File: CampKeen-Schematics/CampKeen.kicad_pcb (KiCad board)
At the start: 4 copper layers, 193.7 x 142.2 mm, 326 parts, among them IC1 CD74HC4050ME4, IC10 SN7404DR, IC11 LTV-814, IC12 LTV-814, IC2 LM2597MX-ADJ_NOPB, IC3 LM2670SX-5.0_NOPB, IC4 DS3231SN#, IC5 OPA2340PA, IC6 OPA2340PA, IC7 SN7404DR, IC8 SN7404DR, IC9 SN7404DR, J1 Vin, J2 Conn_01x02, J3 CircuitSetupsSplitPhase, J4 Conn_01x02, J5 Conn_01x02, J6 Conn_01x02, J7 GenEnclosure, J8 GenHeadL, J9 GenHeadR, P1 Power, P10 CONN_01X01, P11 CONN_01X01, P12 CONN_01X01, P13 CONN_01X01, P2 Analog, P3 Analog, P4 Digital, P5 PWM, P6 PWM, P7 Communication, P8 CONN_01X01, P9 CONN_01X01, Q1 IRF9Z34NPBF, Q10 2N7000, Q11 IRF9Z34NPBF, Q12 2N7000, Q13 2N7000, Q14 2N7000, Q15 2N7000, Q16 2N7000, Q17 2N7000, Q18 2N7000, Q19 2N7000, Q2 2N7000, Q20 2N7000, Q21 2N7000, Q22 2N7000, Q23 2N7000, Q24 2N7000, Q25 2N7000, Q26 2N7000, Q27 2N7000, Q28 2N7000, Q29 2N7000, Q3 IRF9Z34NPBF, Q30 2N7000, Q31 2N7000, Q32 IRF9Z34NPBF, Q33 IRF9Z34NPBF, Q34 2N7000, Q35 IRF9Z34NPBF, Q36 2N7000, Q37 IRF9Z34NPBF, Q38 2N7000, Q39 IRF9Z34NPBF, Q4 2N7000, Q40 2N7000, Q41 IRF9Z34NPBF, Q42 2N7000, Q43 2N7000, Q44 IRF9Z34NPBF, Q45 IRF9Z34NPBF, Q46 2N7000, Q47 IRF9Z34NPBF, Q48 2N7000, Q49 IRF9Z34NPBF, Q5 2N7000, Q50 2N7000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

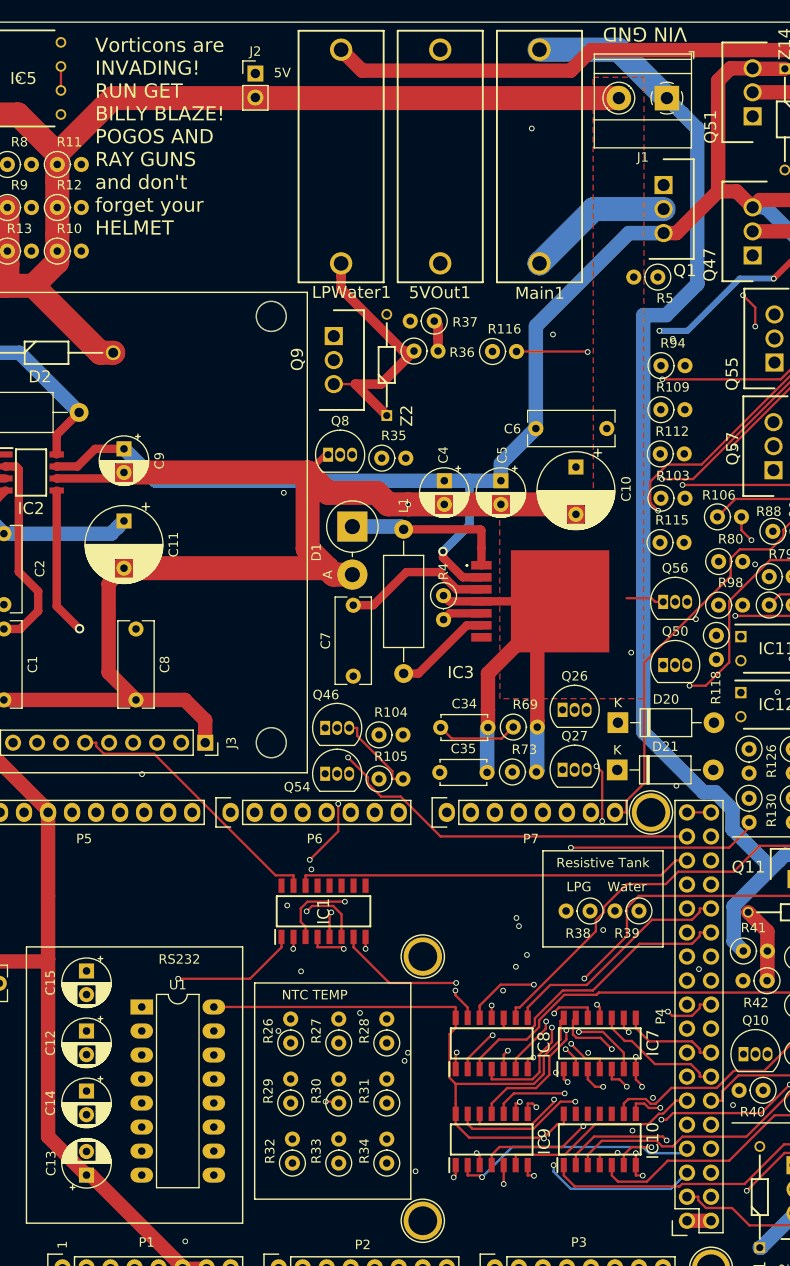
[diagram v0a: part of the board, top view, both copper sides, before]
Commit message: working on fixing some traces for the next HW build.
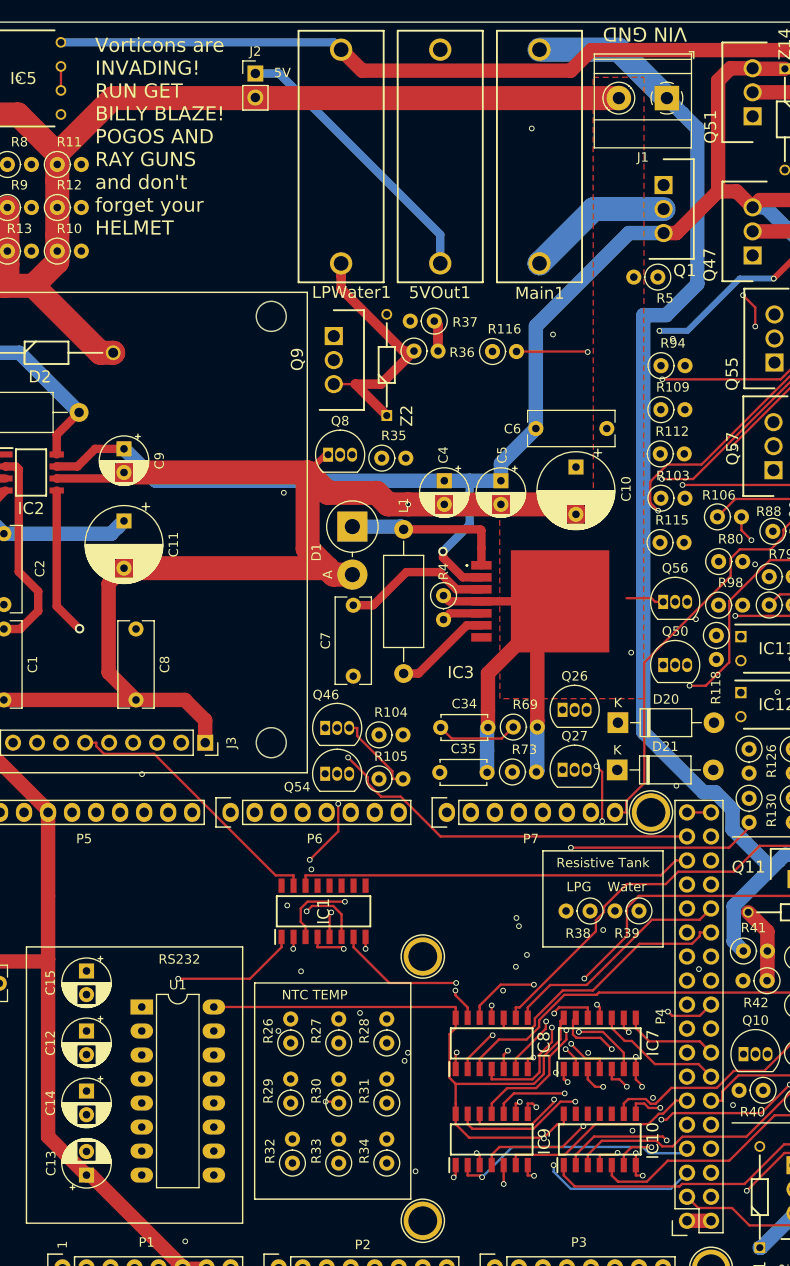
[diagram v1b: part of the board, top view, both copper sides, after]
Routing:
- net +5V: track 844.5 -> 870.3 mm

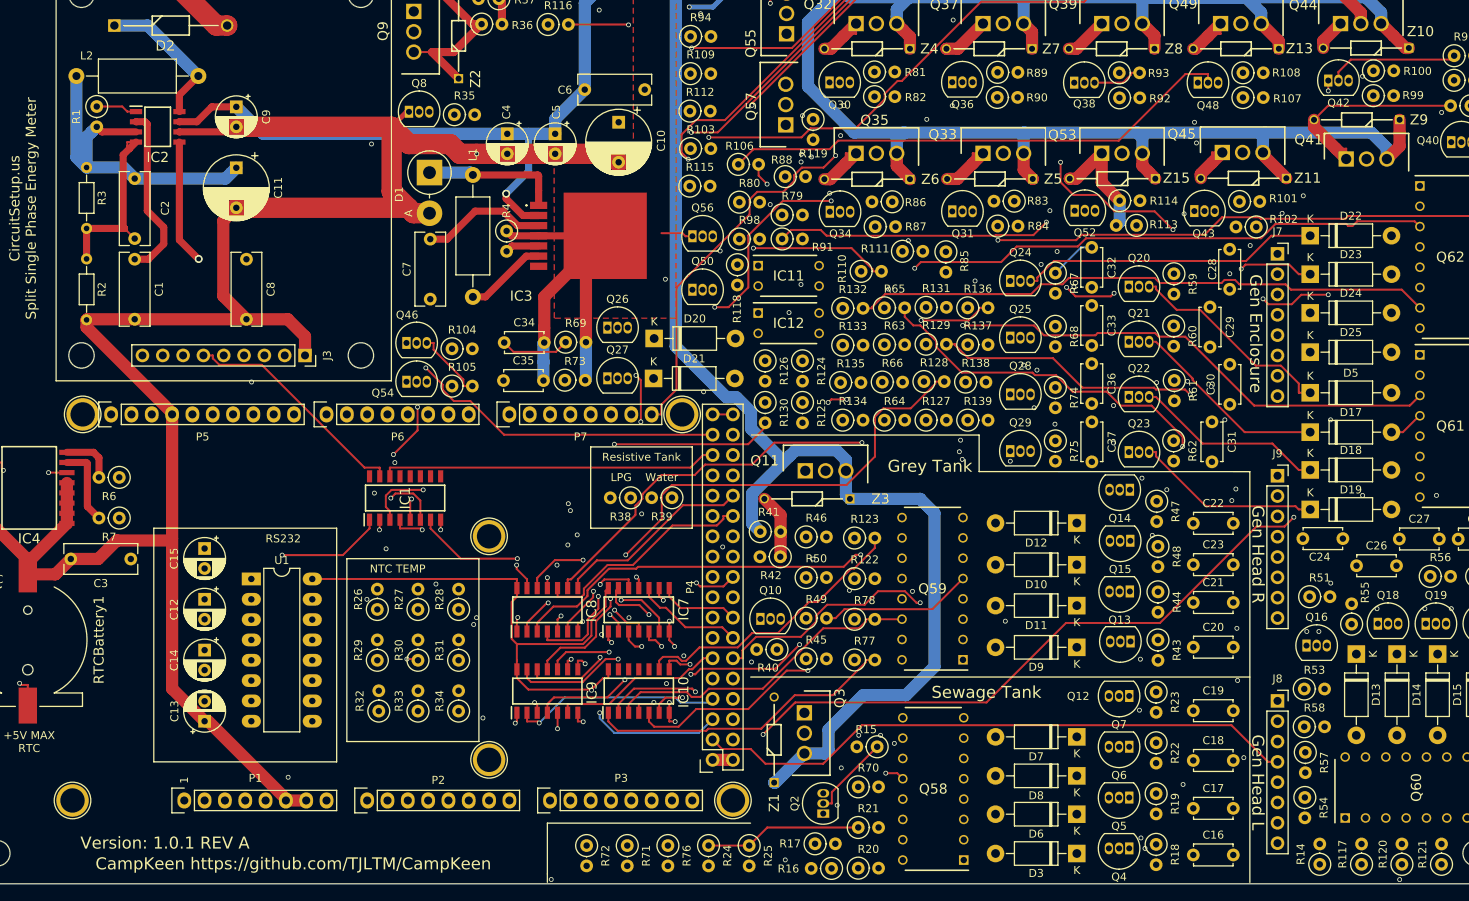
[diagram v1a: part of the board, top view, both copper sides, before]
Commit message: removing the old fab file zips, updated PCB to 1.0.1 Rev B and adding the new fab files.
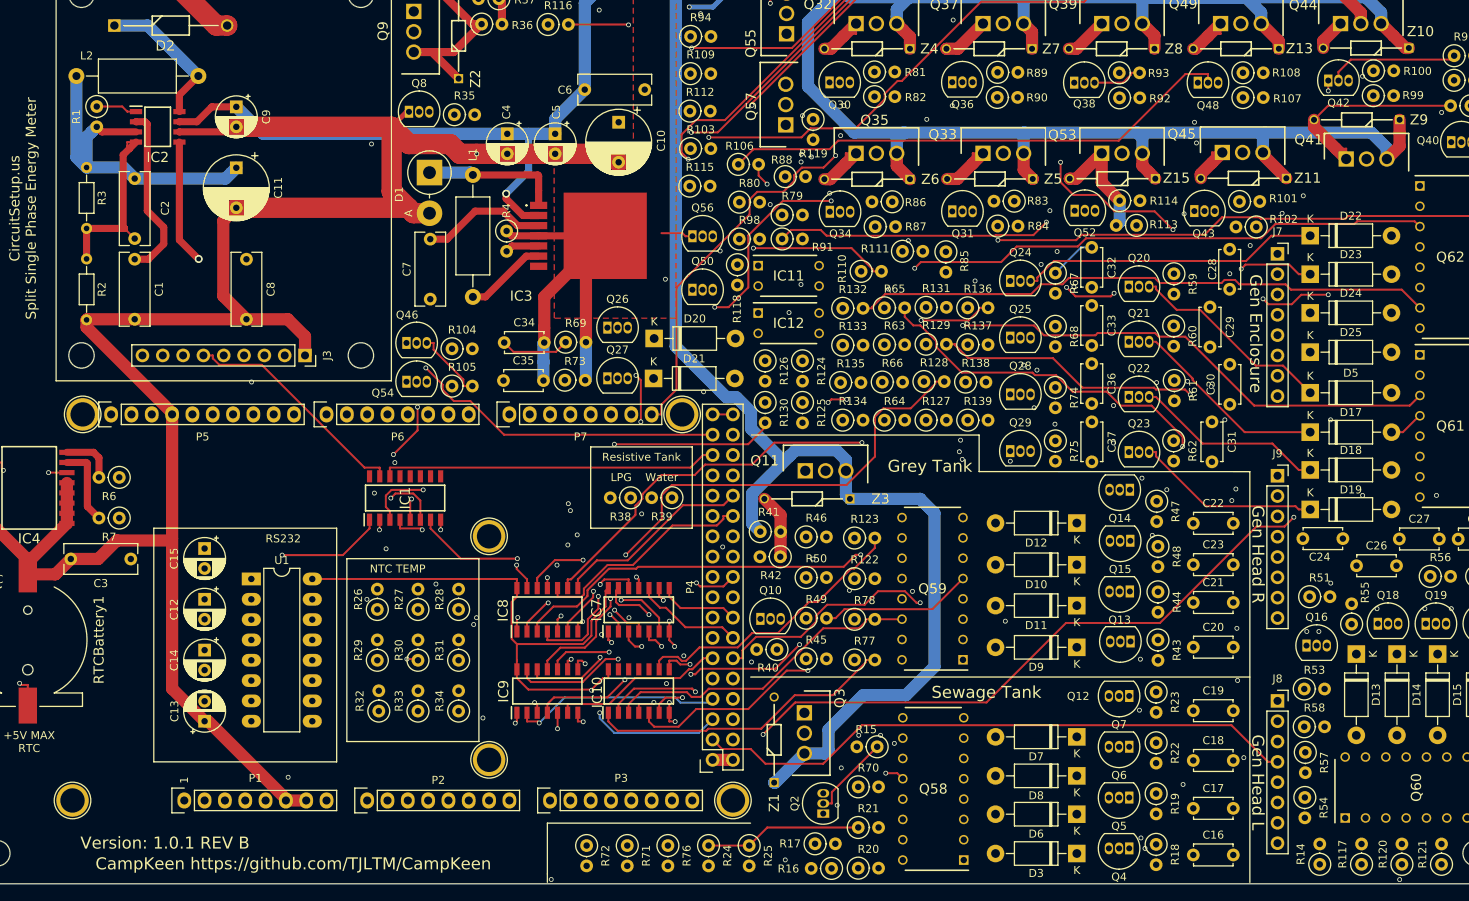
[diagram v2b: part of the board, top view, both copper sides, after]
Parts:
- IC10, IC7, IC8, IC9: footprint Samac_Sys:SOIC127P600X175-14N -> SamacSys_Parts:SOIC127P600X175-14N
- IC11, IC12: footprint Samac_Sys:DIP762W60P254L460H450Q4N -> SamacSys_Parts:DIP762W60P254L460H450Q4N
- Q58, Q59, Q60, Q61, Q62: footprint Samac_Sys:DIP762W60P254L1984H450Q16N -> SamacSys_Parts:DIP762W60P254L1984H450Q16N
- R6, R7: value 47k -> 10k
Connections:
- net AUXVoltage renamed GenFuelPressure
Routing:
- net Net-(D5-Pad1): track 26.5 -> 25.8 mm
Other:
- board text added: "Version: 1.0.1 REV B"
- board text removed: "Version: 1.0.1 REV A"

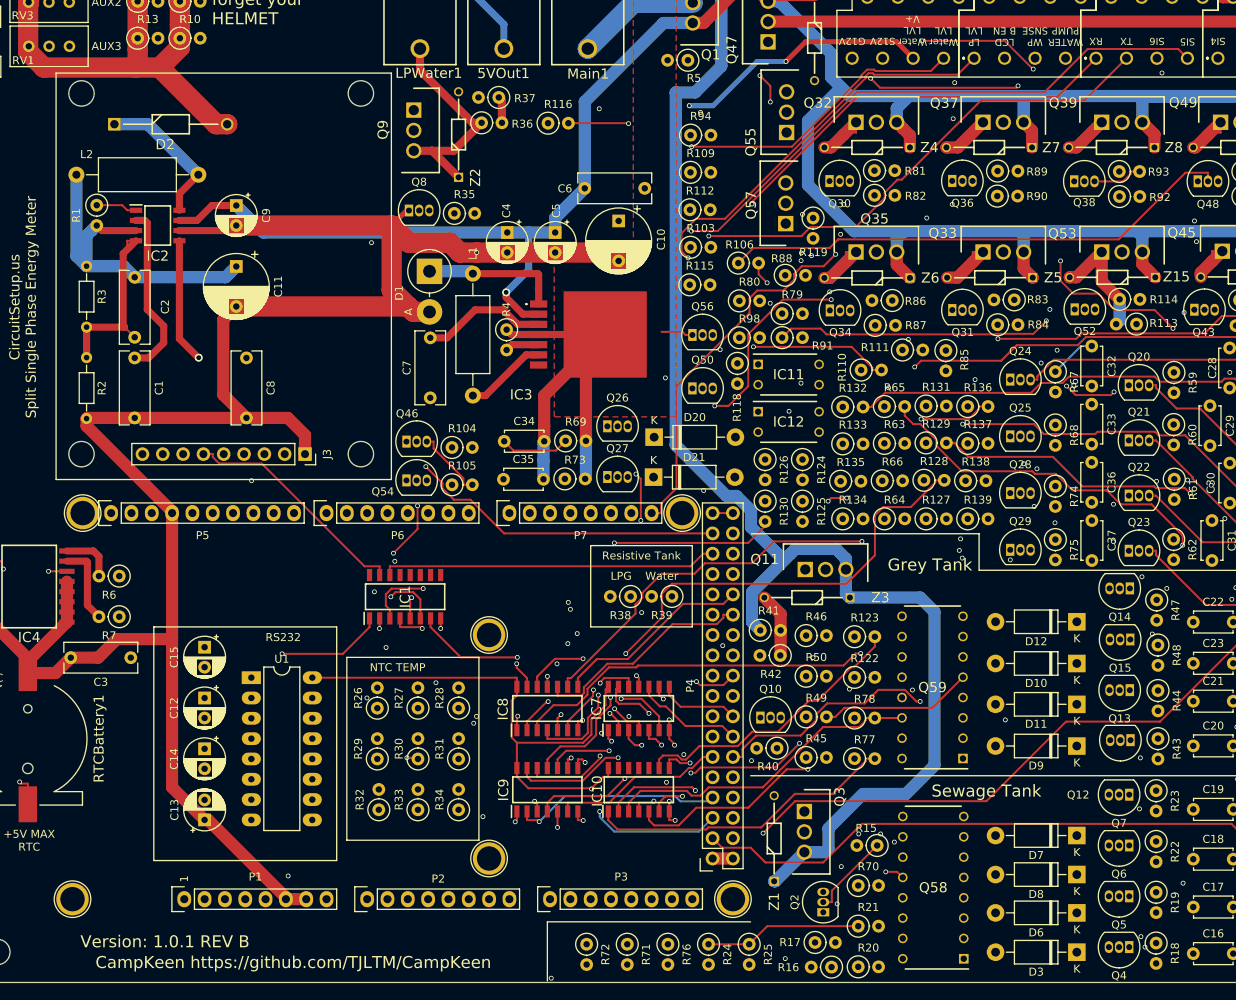
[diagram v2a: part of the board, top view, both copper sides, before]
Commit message: removed from schematic - lcd backlight enable - lcd backlight out - moving gpio around to get free serial pins.
starting to remove the parts from the PCB
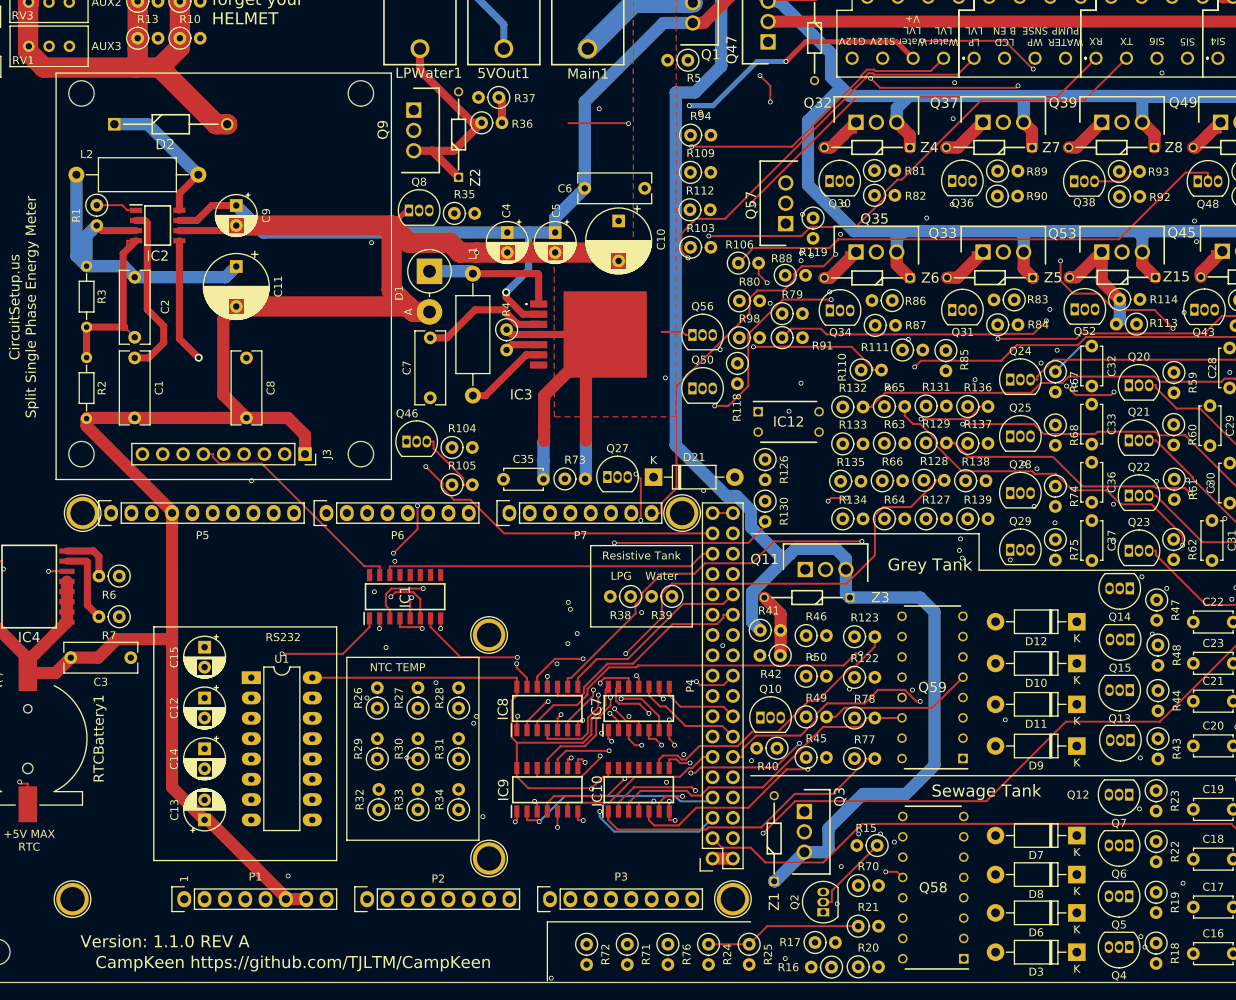
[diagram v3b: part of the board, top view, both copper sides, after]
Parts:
- removed C34: 22nF, Capacitor_THT:C_Disc_D4.7mm_W2.5mm_P5.00mm
- removed D20: 1N4007, Diode_THT:D_DO-41_SOD81_P10.16mm_Horizontal
- removed IC11: LTV-814, SamacSys_Parts:DIP762W60P254L460H450Q4N
- removed Q26, Q54: 2N7000, Package_TO_SOT_THT:TO-92_Inline
- removed Q55: IRF9Z34NPBF, SamacSys_Parts:TO254P469X1042X1967-3P
- removed R115, R69: 1M, Resistor_THT:R_Axial_DIN0207_L6.3mm_D2.5mm_P2.54mm_Vertical
- removed R116: 100k, Resistor_THT:R_Axial_DIN0207_L6.3mm_D2.5mm_P2.54mm_Vertical
- removed R124: 330, Resistor_THT:R_Axial_DIN0207_L6.3mm_D2.5mm_P2.54mm_Vertical
- removed R125: 22k, Resistor_THT:R_Axial_DIN0207_L6.3mm_D2.5mm_P2.54mm_Vertical
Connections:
- net A1 renamed IO210
- C30 pad 1: IO27 -> IO31
- IC8 pad 1: /Inputs/LCDBackLIGHTTTL -> unconnected-(IC8-Pad1)
- IC8 pad 2: LCBBACK -> unconnected-(IC8-Pad2)
- P4 pad 18: LCBBACK -> SO6
- P5 pad 10: LCDBL -> SO5
- P7 pad 1: SO5 -> ESPCOMTXTTL5V
- P7 pad 2: SO6 -> ESPCOMRXTTL5V
- Q22 pad 2: IO27 -> IO31
- Q61 pad 12: /Inputs/LCDBackLIGHTTTL -> /Inputs/SP5TTL
- R128 pad 2: /Inputs/LCDBackLIGHTTTL -> /Inputs/SP5TTL
- R61 pad 1: IO27 -> IO31
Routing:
- net /Inputs/LCDBackLIGHTTTL: track 143.5 -> 0.00 mm, vias 2 -> 0
- net (no net): track 0.00 -> 105.6 mm, vias 0 -> 1
- net IO27: track 98.8 -> 0.00 mm, vias 1 -> 0
- net IO31: track 116.5 -> 33.3 mm
- net Net-(Q54-Pad3): track 80.9 -> 0.00 mm, vias 1 -> 0
- net /Inputs/SP5TTL: track 76.4 -> 143.5 mm, vias 1 -> 2
- net LCDBL: track 63.0 -> 0.00 mm
- net unconnected-(IC8-Pad2): track 0.00 -> 28.6 mm, vias 0 -> 1
- net LCBBACK: track 28.6 -> 0.00 mm, vias 1 -> 0
- net Net-(IC11-Pad1): track 17.0 -> 0.00 mm
- net Net-(D20-Pad2): track 7.74 -> 0.00 mm
- net GND: track 1470.4 -> 1463.1 mm
- net Net-(D20-Pad1): track 4.06 -> 0.00 mm
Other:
- board text added: "Version: 1.1.0 REV A"
- board text removed: "Version: 1.0.1 REV B"

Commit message: adding the EXP32 stuff.
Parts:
- added J10: Conn_01x19, Connector_PinSocket_2.54mm:PinSocket_1x19_P2.54mm_Vertical, F.Cu at (339.3, 148.4)
- added J11: Conn_01x19, Connector_PinSocket_2.54mm:PinSocket_1x19_P2.54mm_Vertical, F.Cu at (332.2, 148.4)
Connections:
- net A2 renamed IO11
- IC1 pad 10: unconnected-(IC1-Pad10) -> EspRX
- IC1 pad 9: unconnected-(IC1-Pad9) -> ESPCOMTXTTL5V

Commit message: cleaned up the PCB changes by removing the old traces and vias from pin swaps got the ESP socket grouped and space correctly need to move some things around to get it onto the board.
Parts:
- moved J10 316.2 mm to (30.3, 215.2), turned to 90 degrees
- moved J11 305.1 mm to (30.3, 192.4), turned to 90 degrees
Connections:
- net IO11 renamed A2
- Q57 pad 3: +5V -> +12V
- R119 pad 1: +5V -> +12V
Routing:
- net +5V: track 870.3 -> 750.2 mm, vias 2 -> 1
- net (no net): track 105.6 -> 0.00 mm, vias 1 -> 0
- net SO5: track 103.1 -> 0.00 mm
- net SO6: track 100.6 -> 0.00 mm, vias 1 -> 0
- net IO49: track 75.0 -> 0.00 mm
- net /Inputs/SP5TTL: track 143.5 -> 71.3 mm, vias 2 -> 0
- net GND: track 1463.1 -> 1400.2 mm
- net unconnected-(IC8-Pad2): track 28.6 -> 0.00 mm, vias 1 -> 0
- net IO31: track 33.3 -> 13.7 mm, vias 1 -> 0
